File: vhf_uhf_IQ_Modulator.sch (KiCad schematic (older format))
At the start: 82 parts

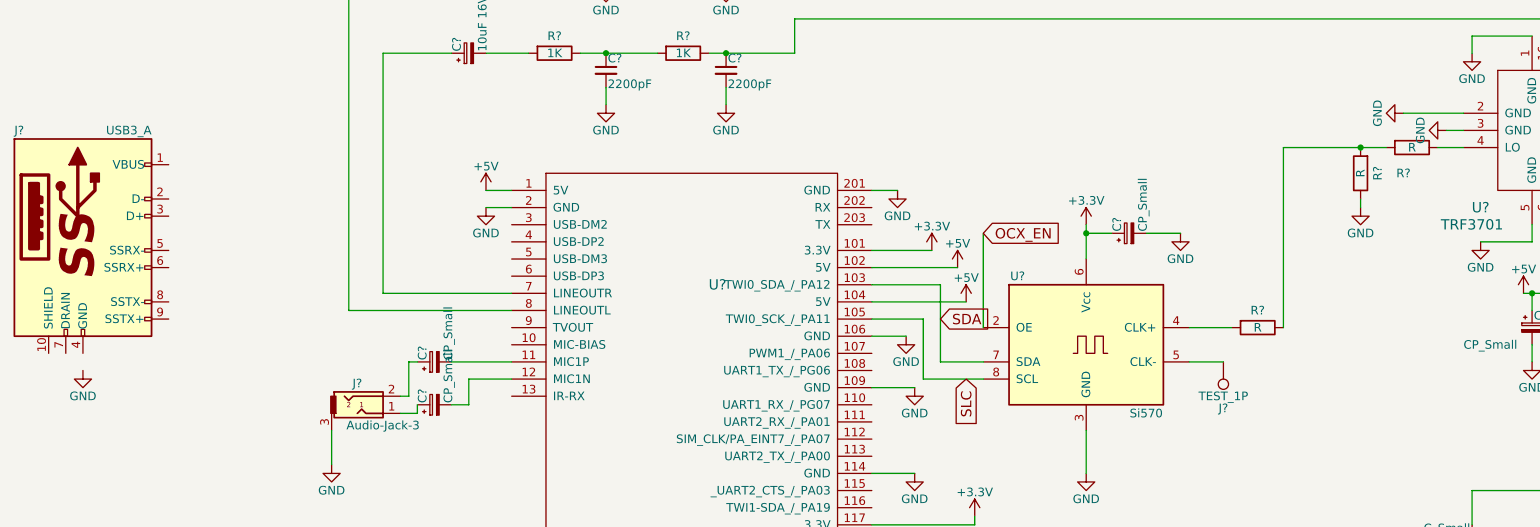
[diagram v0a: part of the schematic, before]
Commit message: 2m filter
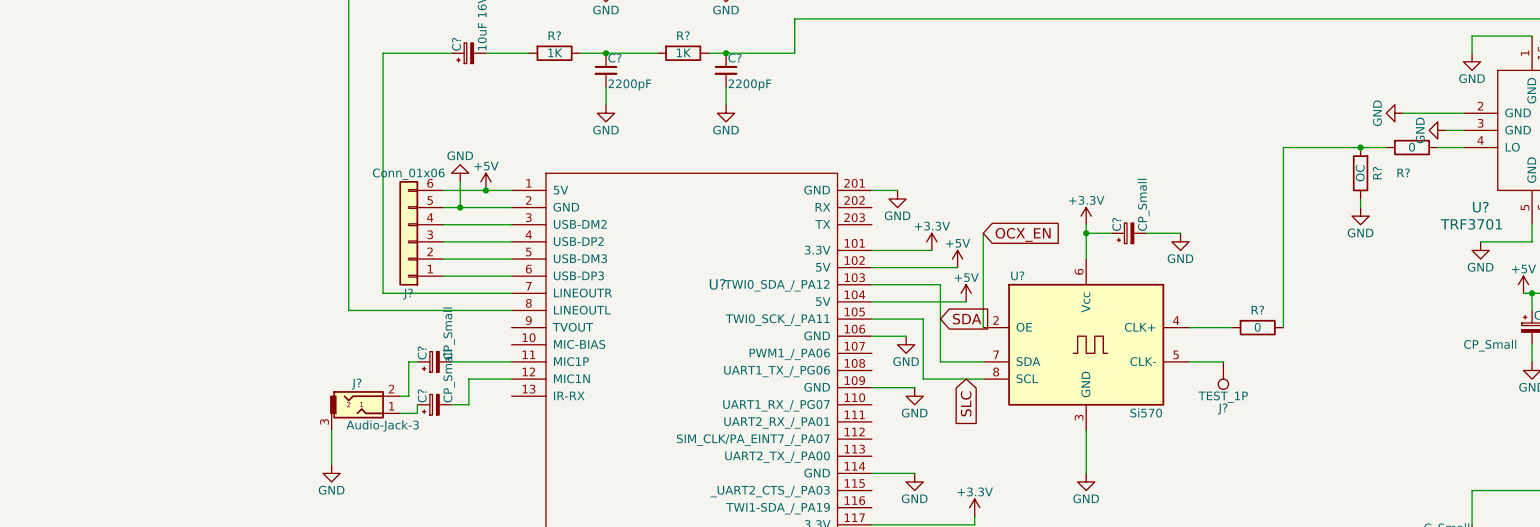
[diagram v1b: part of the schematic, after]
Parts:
- removed J?: USB3_A, symbol USB3_A
- added J?: Conn_01x06, symbol Conn_01x06
- R? (x2): value R -> 0
- R?: value R -> OC
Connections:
- net +5V: now also J?.6 (Pin_6)
- net GND: now also J?.5 (Pin_5)
- net at U?.3 (USB-DM2): now also J?.4 (Pin_4)
- net at U?.4 (USB-DP2): now also J?.3 (Pin_3)
- net at U?.5 (USB-DM3): now also J?.2 (Pin_2)
- net at U?.6 (USB-DP3): now also J?.1 (Pin_1)
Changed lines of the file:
@@
 Sheet 1 1
 Title "IQ modulator 300 to 1.5Ghz"
-Date "2017-11-01"
+Date "2018-06-01"
 Rev "V1.0"
 Comp "Giga Technology"
 Comment1 "This Board is a an RF transmitter board for VHF and UHF"
-Comment2 ""
+Comment2 "2m and 70cm filter"
 Comment3 ""
 Comment4 ""
@@
 P 7950 3850
 F 0 "R?" V 7850 3850 50  0000 C CNN
-F 1 "R" V 7950 3850 50  0000 C CNN
+F 1 "0" V 7950 3850 50  0000 C CNN
 F 2 "" V 7880 3850 50  0001 C CNN
 F 3 "" H 7950 3850 50  0001 C CNN
@@
 P 8850 2800
 F 0 "R?" V 9000 2750 50  0000 C CNN
-F 1 "R" V 8850 2800 50  0000 C CNN
+F 1 "0" V 8850 2800 50  0000 C CNN
 F 2 "" V 8780 2800 50  0001 C CNN
 F 3 "" H 8850 2800 50  0001 C CNN
@@
 P 8550 2950
 F 0 "R?" V 8450 2950 50  0000 C CNN
-F 1 "R" V 8550 2950 50  0000 C CNN
+F 1 "OC" V 8550 2950 50  0000 C CNN
 F 2 "" V 8480 2950 50  0001 C CNN
 F 3 "" H 8550 2950 50  0001 C CNN
@@
 $EndComp
 $Comp
-L USB3_A J?
-U 1 1 5A1CD0DE
-P 1100 3300
-F 0 "J?" H 700 3900 50  0000 L CNN
-F 1 "USB3_A" H 1500 3900 50  0000 R CNN
-F 2 "" H 1250 3400 50  0000 C CNN
-F 3 "" H 1250 3400 50  0000 C CNN
-	1    1100 3300
-	1    0    0    -1
-$EndComp
-$Comp
-L GND #PWR?
-U 1 1 5A1CFCE0
-P 1100 4100
-F 0 "#PWR?" H 1100 3850 50  0001 C CNN
-F 1 "GND" H 1100 3950 50  0000 C CNN
-F 2 "" H 1100 4100 50  0001 C CNN
-F 3 "" H 1100 4100 50  0001 C CNN
-	1    1100 4100
-	1    0    0    -1
-$EndComp
-$Comp
 L GND #PWR?
 U 1 1 5A1D007B
@@
 L GND #PWR?
 U 1 1 5A1D0577
-P 3450 3150
-F 0 "#PWR?" H 3450 2900 50  0001 C CNN
-F 1 "GND" H 3450 3000 50  0000 C CNN
-F 2 "" H 3450 3150 50  0001 C CNN
-F 3 "" H 3450 3150 50  0001 C CNN
-	1    3450 3150
-	1    0    0    -1
+P 3300 3000
+F 0 "#PWR?" H 3300 2750 50  0001 C CNN
+F 1 "GND" H 3300 2850 50  0000 C CNN
+F 2 "" H 3300 3000 50  0001 C CNN
+F 3 "" H 3300 3000 50  0001 C CNN
+	1    3300 3000
+	-1   0    0    1
 $EndComp
 $Comp
@@
 	5700 3050 5850 3050
 Wire Wire Line
-	3600 3050 3450 3050
-Wire Wire Line
-	3600 3150 3450 3150
+	3200 3050 3600 3050
 Wire Wire Line
 	5700 3700 6250 3700
@@
 Wire Wire Line
 	11900 6550 11900 6650
+$Comp
+L Conn_01x06 J?
+U 1 1 5B1CC859
+P 3000 3350
+F 0 "J?" H 3000 3650 50  0000 C CNN
+F 1 "Conn_01x06" H 3000 2950 50  0000 C CNN
+F 2 "" H 3000 3350 50  0001 C CNN
+F 3 "" H 3000 3350 50  0001 C CNN
+	1    3000 3350
+	-1   0    0    1
+$EndComp
+Wire Wire Line
+	3200 3550 3600 3550
+Wire Wire Line
+	3200 3450 3600 3450
+Wire Wire Line
+	3200 3350 3600 3350
+Wire Wire Line
+	3200 3250 3600 3250
+Wire Wire Line
+	3200 3150 3600 3150
+Connection ~ 3450 3050
+Wire Wire Line
+	3300 3000 3300 3150
+Connection ~ 3300 3150
 $EndSCHEMATC

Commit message: finilising Digarm
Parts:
- removed C? (x2): C_Small, symbol C_Small
- removed J?: Conn_Coaxial, symbol Conn_Coaxial
- removed J?: Conn_01x03, symbol Conn_01x03
- removed R? (x3): R, symbol R
- removed U?: SBB-2089, symbol SBB-2089
- removed U?: SF434E_SAW433.92Mhz, symbol SF434E_SAW433.92Mhz
- added C? (x2): 1uF 16V, symbol CP
- added C?: 100nF, symbol C_Small
- added C?: 10uF 16V, symbol CP_Small
- added J?: CONN_01X04, symbol CONN_01X04
- added Q? (x3): BC817-40, TO_SOT_Packages_SMD:SOT-23, symbol BC817-40
- added R? (x2): 6k5, symbol R
- added R? (x2): 10k, symbol R
- added R?: 6k8, symbol R
- C?: value CP_Small -> 4.7uF 16V
- C?: value C_Small -> 220pF
- C?: value C_Small -> 33pF
- C?: value C_Small -> 1nF
- C?: value C_Small -> 27pF
- C?: value C_Small -> 15pF
- C? (x2): value C_Small -> 100pF
- C?: value C_Small -> 3.3pF
- L? (x2): value L -> 33nH
- L? (x2): value L -> 33nF
- L?: value L -> 22nF
- R? (x2): value R -> 0
- R?: value R -> OC
- R?: value R -> 2k2
- R?: value R -> 1k8
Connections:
- net +3V3: now also R?.2
- net +5V: now also U?.5 (VDD), C?.1, C?.1, C?.1, C?.2, J?.1 (P1), R?.1, R?.1, R?.1, R?.2
- net GND: now also U?.2 (VSS), U?.6 (Vin-), C?.1, C?.2, C?.2, C?.2, J?.4 (P4), Q?.2 (E), Q?.2 (E), Q?.2 (E)
- net SDA: now also U?.4 (SDA), R?.2
- net SLC: now also U?.3 (SCL), R?.2
- net at U?.116 (TWI1-SDA_/_PA19): now also J?.2 (P2)
- net at U?.118 (TWI1-SCK_/_PA18): now also J?.3 (P3)
- net at C?.2, L?.2, U?.7 (VCC2/RFout)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: now also U?.8 (VCC2/RFout)
- net at C?.1: now also R?.2
- net OCX_EN: no longer names the net of U?.2 (OE)
- net OCX_EN: now also Q?.3 (C), R?.1
- net PA_ON: no longer names the net of U?.10 (Pow_Down)
- net PA_ON: now also Q?.3 (C), R?.1
- net PowerDown: no longer names the net of U?.7 (PWD)
- net PowerDown: now also Q?.3 (C), R?.2
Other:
- note removed: "70cm BPF"
- note removed: "Check connection\n"
- moved on the sheet: C?, J?, L?, R?

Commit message: Done Anotation
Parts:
- added C14: 1nF, symbol C_Small
- added R17, R8: 6k8, symbol R
- C15, C20: renamed from C?; value CP_Small -> 1uF 16V
- C23: renamed from C?; value CP_Small -> 10uF 16V
- C29, C30, C31: renamed from C?; value C_Small -> 33pF
- J5: renamed from J?; value Conn_Coaxial -> SMA Edge FM
- L6, L9: renamed from L?; value L -> 56nH
- L7, L8: renamed from L?; value L -> 110nH
- R20, R21, R22, R23: renamed from R?; value R -> 0
- R24, R25: renamed from R?; value R -> OC
- gave numbers to parts that had none: 69
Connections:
- net +5V: now also C14.2
- net GND: now also C14.1
- net INT: now also U4.126 (SIM_DET/PA_EINT10_/_PA10)
- net PA06: now reaches U4.107 (PWM1_/_PA06)
- net PA06: now also R8.1
- net PA01: now reaches U4.111 (UART2_RX_/_PA01)
- net PA01: now also Q1.1 (B)
- net PA07: now reaches U4.112 (SIM_CLK/PA_EINT7_/_PA07)
- net PA07: now also R17.1
- net at Q2.1 (B): now also R8.2
- net at Q3.1 (B): now also R17.2
- no-connect marks 1 -> 16
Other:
- moved on the sheet: C1, C17, J2, L1, R12, U3

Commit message: Allocated Footprints
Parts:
- BT1: footprint (none) -> Battery_Holders:Keystone_103_1x20mm-CoinCell
- C1, C13, C15, C20: footprint (none) -> Capacitors_Tantalum_SMD:CP_Tantalum_Case-R_EIA-2012-12_Reflow
- C10, C11, C12, C14, C16, C18, C19, C21, C22, C23, C24, C26, C27, C29, C30, C31, C32, C33, C4, C5, C6, C7, C8, C9, L1, L3, L5: footprint (none) -> Capacitors_SMD:C_0805_HandSoldering
- C17, C2, C3: value CP_Small -> 1uF 16V; footprint (none) -> Capacitors_Tantalum_SMD:CP_Tantalum_Case-R_EIA-2012-12_Reflow
- C25: value CP_Small -> 10uF 16V; footprint (none) -> Capacitors_SMD:C_0805_HandSoldering
- C28: value C_Small -> 220pF; footprint (none) -> Capacitors_SMD:C_0805_HandSoldering
- D1: footprint (none) -> Diodes_SMD:D_SOD-123
- J1: footprint (none) -> Connectors_Molex:Molex_KK-6410-06_06x2.54mm_Straight
- J2, L2, L4, L6, L7, L8, L9: footprint (none) -> Inductors_SMD:L_0805_HandSoldering
- J3: footprint (none) -> Connectors_Molex:Molex_KK-6410-03_03x2.54mm_Straight
- J4: footprint (none) -> Connectors_Molex:Molex_KK-6410-04_04x2.54mm_Straight
- J5: footprint (none) -> Connectors_Molex:Molex_SMA_Jack_Edge_Mount
- R1, R10, R11, R12, R13, R14, R15, R16, R17, R18, R19, R2, R20, R21, R22, R23, R24, R25, R26, R27, R28, R3, R4, R5, R6, R7, R8, R9, RV1, RV2, U2: footprint (none) -> Resistors_SMD:R_0805_HandSoldering
- U1: footprint (none) -> Housings_VQFN:VQFN-16_3x3mm
- U4: footprint (none) -> orangepi-zero:orangepi-zero
- U5: footprint (none) -> TO_SOT_Packages_SMD:SOT-23-6_Handsoldering
- U6: footprint (none) -> Housing_SO8:SO-8
- Y1: footprint (none) -> Crystals:Crystal_SMD_G8-2pin_3.2x1.5mm_HandSoldering
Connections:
- no-connect marks 16 -> 15
